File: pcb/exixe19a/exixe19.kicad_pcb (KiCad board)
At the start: 2 copper layers, 20 x 40 mm, 39 parts, among them J1 Conn_01x07, J2 Conn_01x07, Q1 BF820W, Q10 BF820W, Q11 BF820W, Q3 MSB92W, Q4 BF820W, Q5 BF820W, Q6 BF820W, Q7 BF820W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

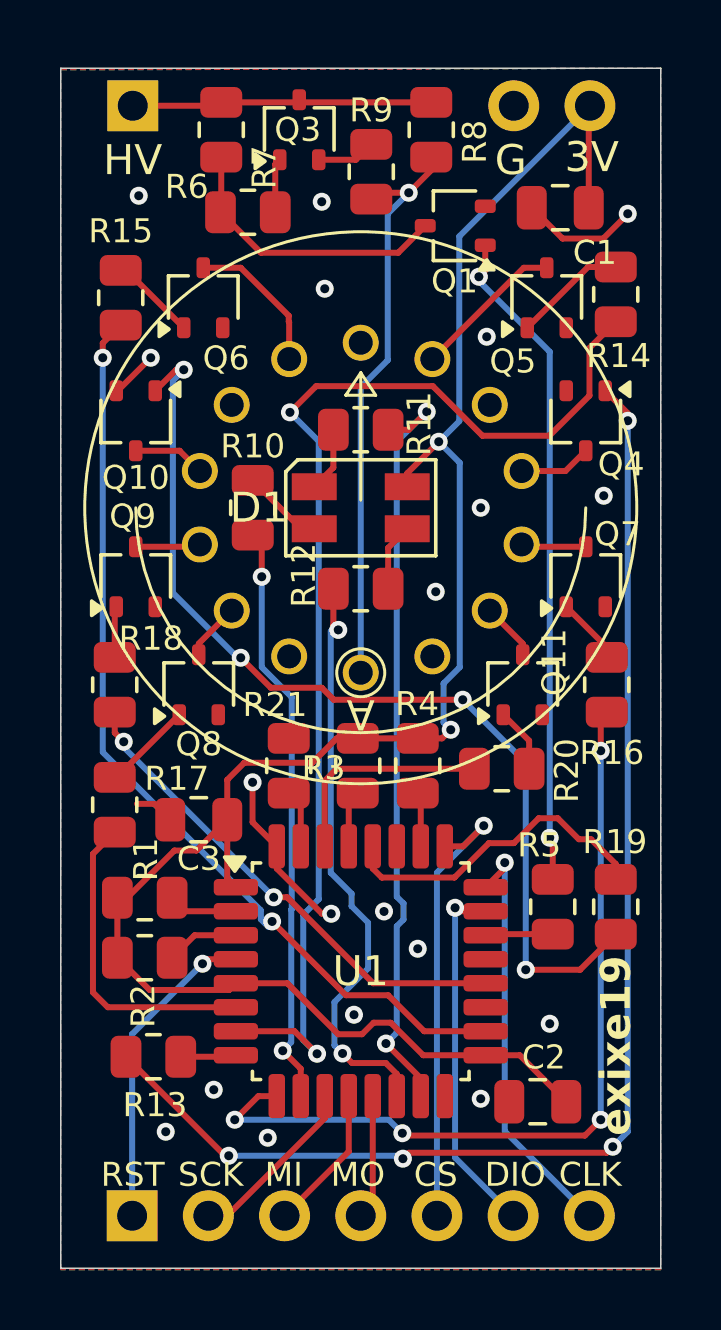
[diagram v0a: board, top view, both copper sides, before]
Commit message: Tidied up IN-19, started update to IN-14 board
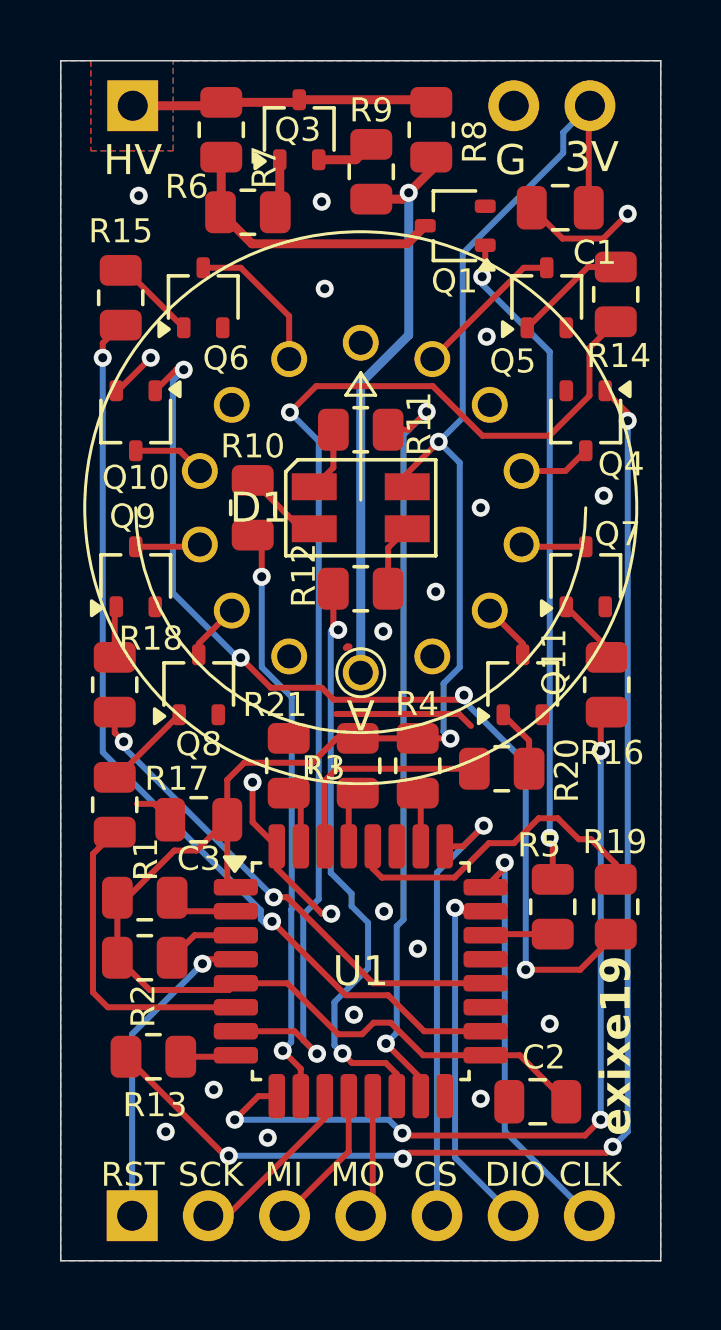
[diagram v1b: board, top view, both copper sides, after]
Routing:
- net GND: track 12.6 -> 17.4 mm, vias 19 -> 20

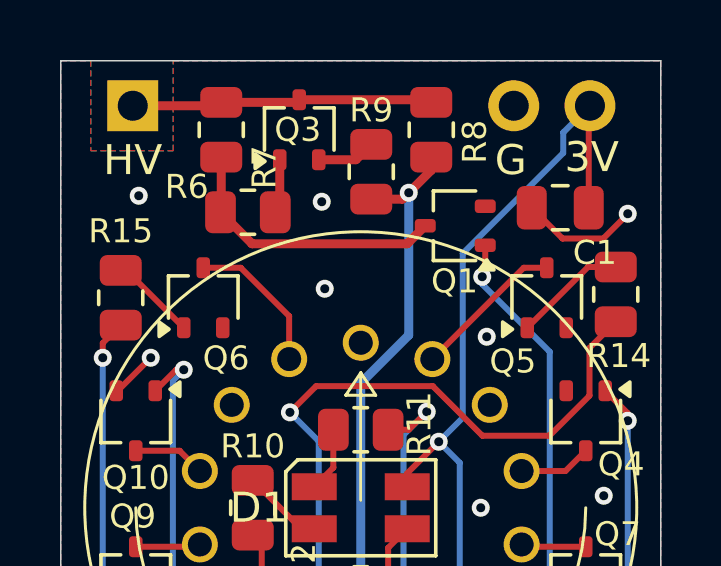
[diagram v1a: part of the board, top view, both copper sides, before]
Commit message: attempt to correct firmware to remove glowing led issue
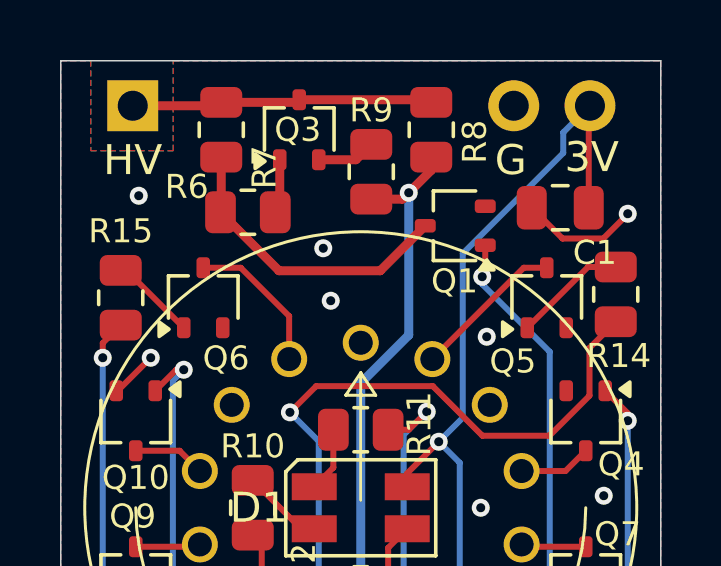
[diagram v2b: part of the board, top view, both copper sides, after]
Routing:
- net Net-(Q1-C): track 9.36 -> 10.1 mm
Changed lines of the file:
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@@
 			(net 25 "+HV")
 			(pintype "passive")
+			(clearance 0.5)
 		)
 		(pad "2" smd roundrect
@@
 			(net 6 "Net-(J1-Pin_1)")
 			(pintype "passive")
+			(clearance 0.5)
 		)
 		(pad "2" smd roundrect
@@
 			(net 28 "Net-(Q1-C)")
 			(pintype "passive")
+			(clearance 0.5)
 		)
 		(embedded_fonts no)
@@
 			(pinfunction "B")
 			(pintype "input")
+			(clearance 0.5)
 		)
 		(pad "2" smd roundrect
@@
 			(pinfunction "E")
 			(pintype "passive")
+			(clearance 0.5)
 		)
 		(pad "3" smd roundrect
@@
 			(pinfunction "C")
 			(pintype "passive")
+			(clearance 0.5)
 		)
 		(embedded_fonts no)
@@
 			(net 25 "+HV")
 			(pintype "passive")
+			(clearance 0.5)
 		)
 		(pad "2" smd roundrect
@@
 			(net 6 "Net-(J1-Pin_1)")
 			(pintype "passive")
+			(clearance 0.5)
 		)
 		(embedded_fonts no)
@@
 	)
 	(via
-		(at 33 41.4)
+		(at 38.75 37.75)
 		(size 0.6)
 		(drill 0.3)
@@
 	)
 	(via
-		(at 46.3 63.6)
+		(at 33 41.4)
 		(size 0.6)
 		(drill 0.3)
@@
 	)
 	(via
-		(at 38.7 36.2)
+		(at 46.3 63.6)
 		(size 0.6)
 		(drill 0.3)
@@
 	)
 	(via
-		(at 38.8 39.1)
+		(at 39 39.5)
 		(size 0.6)
 		(drill 0.3)
@@
 	)
 	(segment
-		(start 41.549 37.601)
+		(start 40.65 38.5)
 		(end 42.15 37)
 		(width 0.3)
@@
 	)
 	(segment
-		(start 35.325 36.55)
-		(end 36.376 37.601)
+		(start 37.275 38.5)
+		(end 40.65 38.5)
 		(width 0.3)
 		(layer "F.Cu")
@@
 	)
 	(segment
-		(start 36.376 37.601)
-		(end 41.549 37.601)
+		(start 35.325 36.55)
+		(end 37.275 38.5)
 		(width 0.3)
 		(layer "F.Cu")
@@
 		(hatch edge 0.5)
 		(connect_pads
-			(clearance 0.25)
+			(clearance 0.2)
 		)
-		(min_thickness 0.25)
+		(min_thickness 0.2)
 		(filled_areas_thickness no)
 		(fill yes
